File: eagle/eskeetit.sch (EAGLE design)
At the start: 46 parts, among them M1 WIRELESS-NRF24L01, U1 GY-521MPU6050, U2 TPS63000DRCR, Y1 20MHz

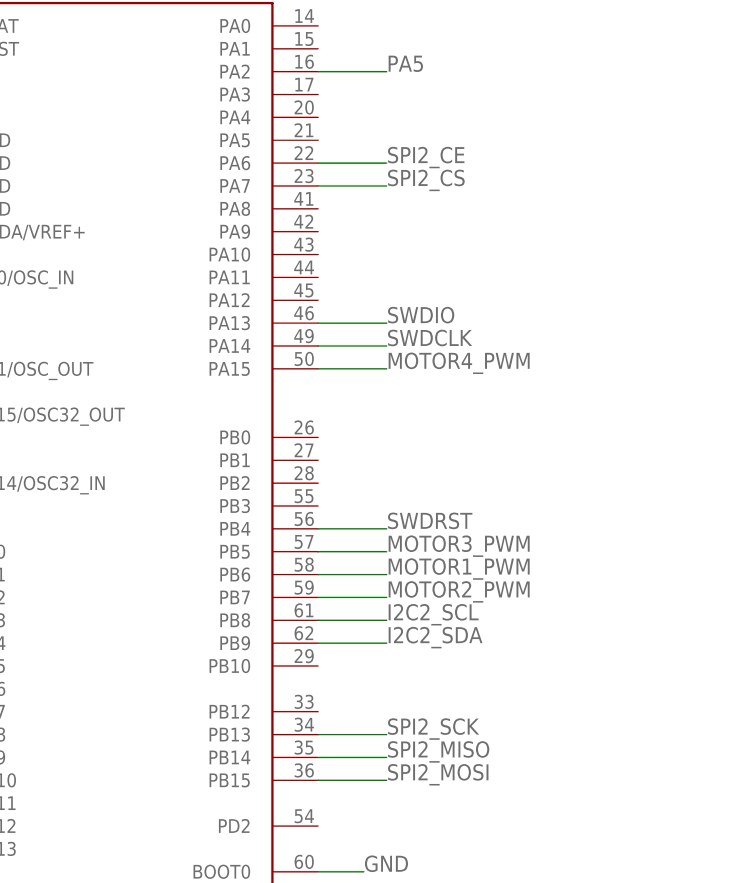
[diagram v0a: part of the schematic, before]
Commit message: leads are roasting us and we are trying to fix
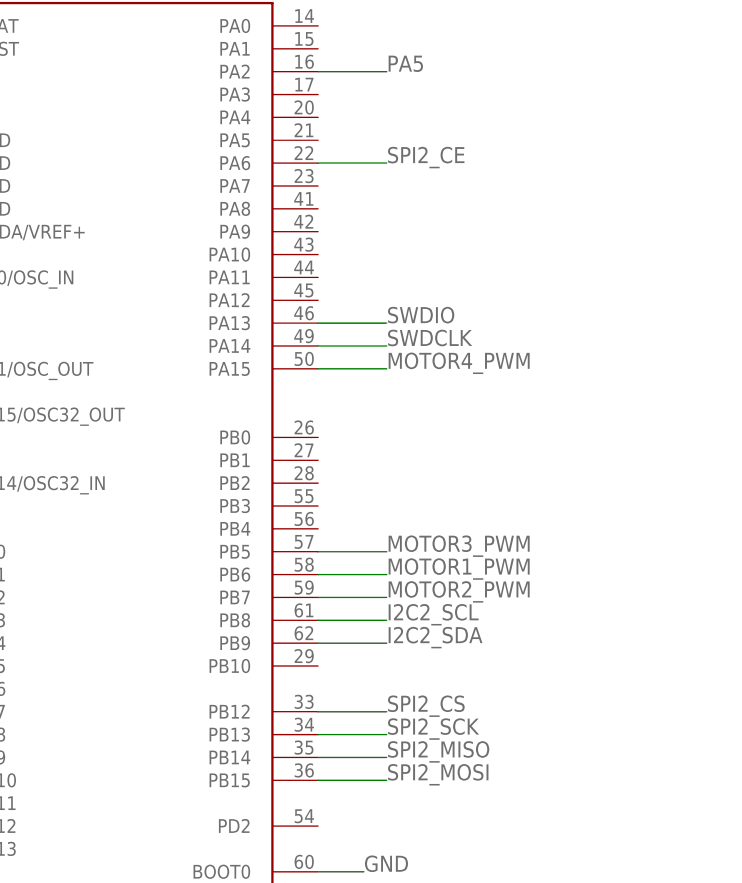
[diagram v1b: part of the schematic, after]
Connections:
- net SPI2_CS: now also U$7.PB12; no longer U$7.PA7
- net SWDRST: no longer U$7.PB4
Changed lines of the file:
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@@
 <net name="SWDRST" class="0">
-<segment>
-<pinref part="U$7" gate="G$1" pin="PB4"/>
-<wire x1="-276.86" y1="172.72" x2="-269.24" y2="172.72" width="0.1524" layer="91"/>
-<label x="-269.24" y="172.72" size="1.778" layer="95"/>
-</segment>
 <segment>
 <pinref part="S1" gate="G$1" pin="2"/>
@@
 <net name="SPI2_CS" class="0">
 <segment>
-<pinref part="U$7" gate="G$1" pin="PA7"/>
-<wire x1="-276.86" y1="210.82" x2="-269.24" y2="210.82" width="0.1524" layer="91"/>
-<label x="-269.24" y="210.82" size="1.778" layer="95"/>
-</segment>
-<segment>
 <pinref part="M1" gate="G$1" pin="CSN"/>
 <wire x1="-406.4" y1="96.52" x2="-411.48" y2="96.52" width="0.1524" layer="91"/>
 <label x="-419.1" y="96.52" size="1.778" layer="95"/>
 </segment>
+<segment>
+<pinref part="U$7" gate="G$1" pin="PB12"/>
+<wire x1="-276.86" y1="152.4" x2="-269.24" y2="152.4" width="0.1524" layer="91"/>
+<label x="-269.24" y="152.4" size="1.778" layer="95"/>
+</segment>
 </net>
